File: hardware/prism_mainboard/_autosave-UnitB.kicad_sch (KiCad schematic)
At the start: 1 part, among them U1 XC7Z015-2CLG485I

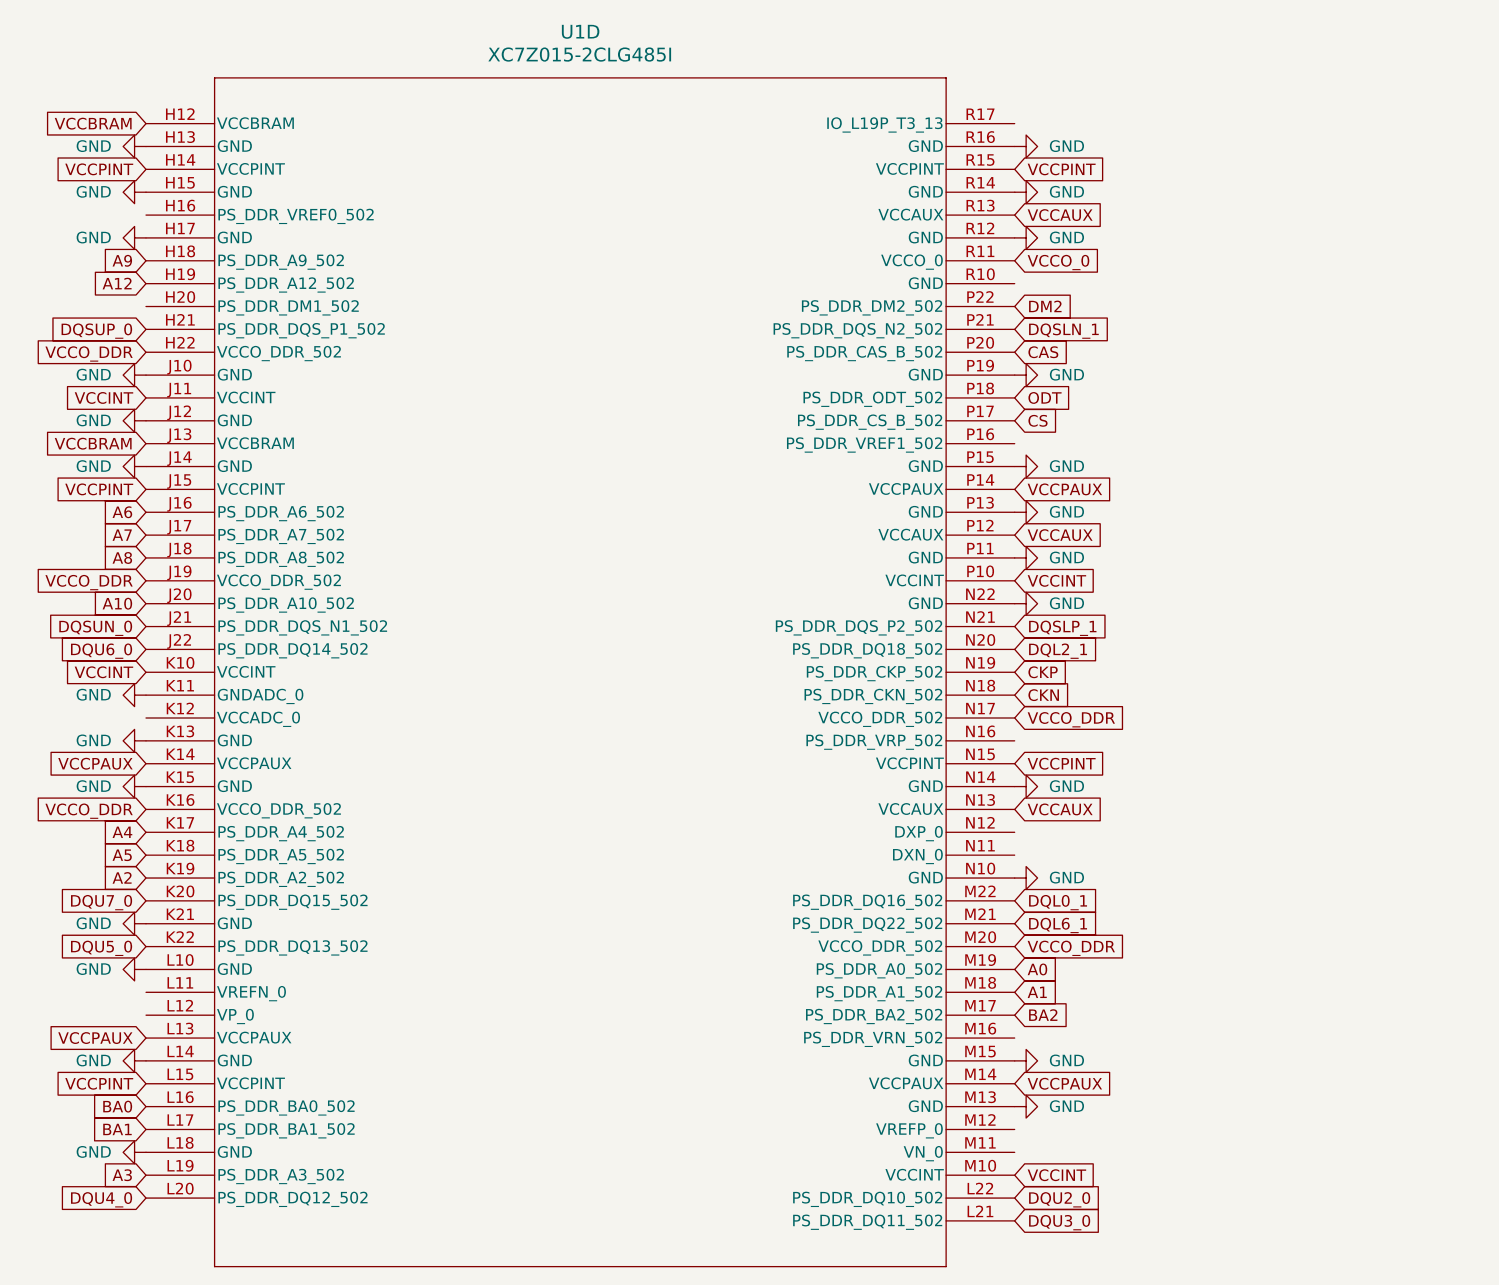
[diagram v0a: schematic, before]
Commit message: Schematic Updates & PCB Population
Populated the PCB with footprints from Main PC, should show up now. Also been updating the KiCAD schematics to connect the DDR3L Modules to the FPGA. Should be done except for a few pins that I'm not sure what they do yet. But Addressing and data pins should be connected correctly now
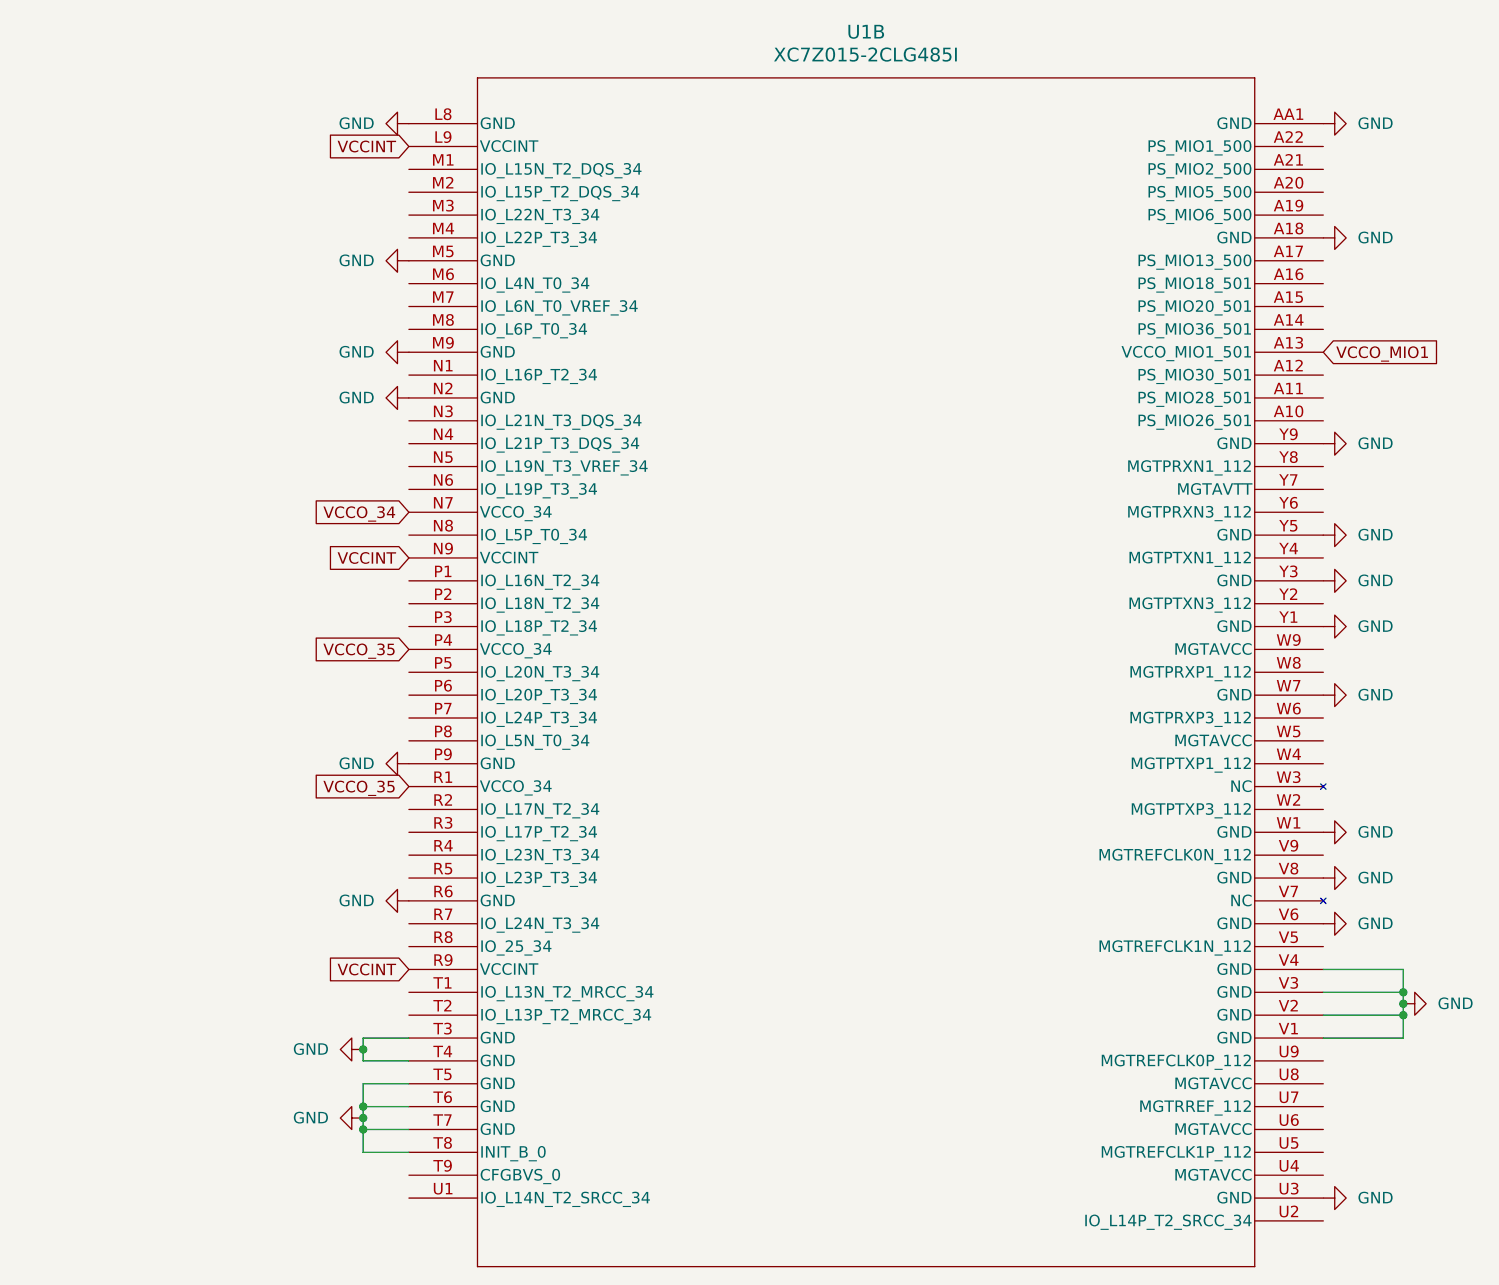
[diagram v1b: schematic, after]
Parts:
- removed U1: XC7Z015-2CLG485I, CLG485_XIL, symbol XC7Z015-CLG485:XC7Z015-2CLG485I
- added U1: XC7Z015-2CLG485I, CLG485_XIL, symbol XC7Z015-CLG485:XC7Z015-2CLG485I
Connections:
- net GND: now also U1.A18 (GND), U1.AA1 (GND), U1.L8 (GND), U1.M5 (GND), U1.M9 (GND), U1.N2 (GND), U1.P9 (GND), U1.R6 (GND), U1.T3 (GND), U1.T4 (GND), U1.T5 (GND), U1.T6 (GND), U1.T7 (GND), U1.T8 (INIT_B_0), U1.U3 (GND), U1.V1 (GND), U1.V2 (GND), U1.V3 (GND), U1.V4 (GND), U1.V6 (GND), U1.V8 (GND), U1.W1 (GND), U1.W7 (GND), U1.Y1 (GND), U1.Y3 (GND), U1.Y5 (GND), U1.Y9 (GND)
- net VCCINT: now also U1.L9 (VCCINT), U1.N9 (VCCINT), U1.R9 (VCCINT)
- new net VCCO_34: U1.N7 (VCCO_34)
- new net VCCO_35: U1.P4 (VCCO_34), U1.R1 (VCCO_34)
- new net VCCO_MIO1: U1.A13 (VCCO_MIO1_501)
